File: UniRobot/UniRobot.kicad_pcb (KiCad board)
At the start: 2 copper layers, 66.5 x 65.5 mm, 11 parts, among them J1 Conn_01x01_Socket, J2 Conn_01x01_Socket, J3 Conn_01x02_Socket, K1 PR23-5V-900-1A, Q1 IRLML6344TRPBF, U1 RFM69HW

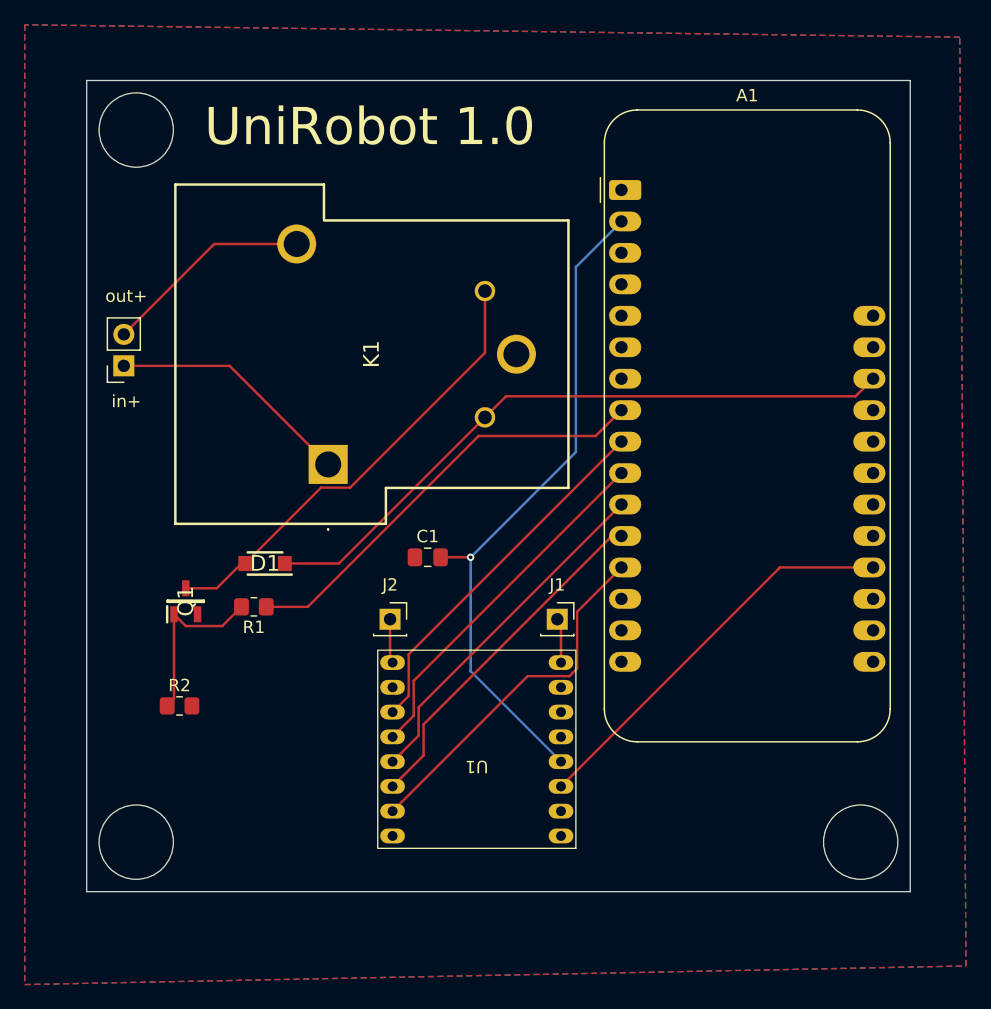
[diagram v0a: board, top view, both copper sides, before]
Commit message: Har lavet begge pcber om. Remote har ændret struktur for mere håndholdt design og ekstra knapper plus LEDer. roboside har fået ny relay og LEDer
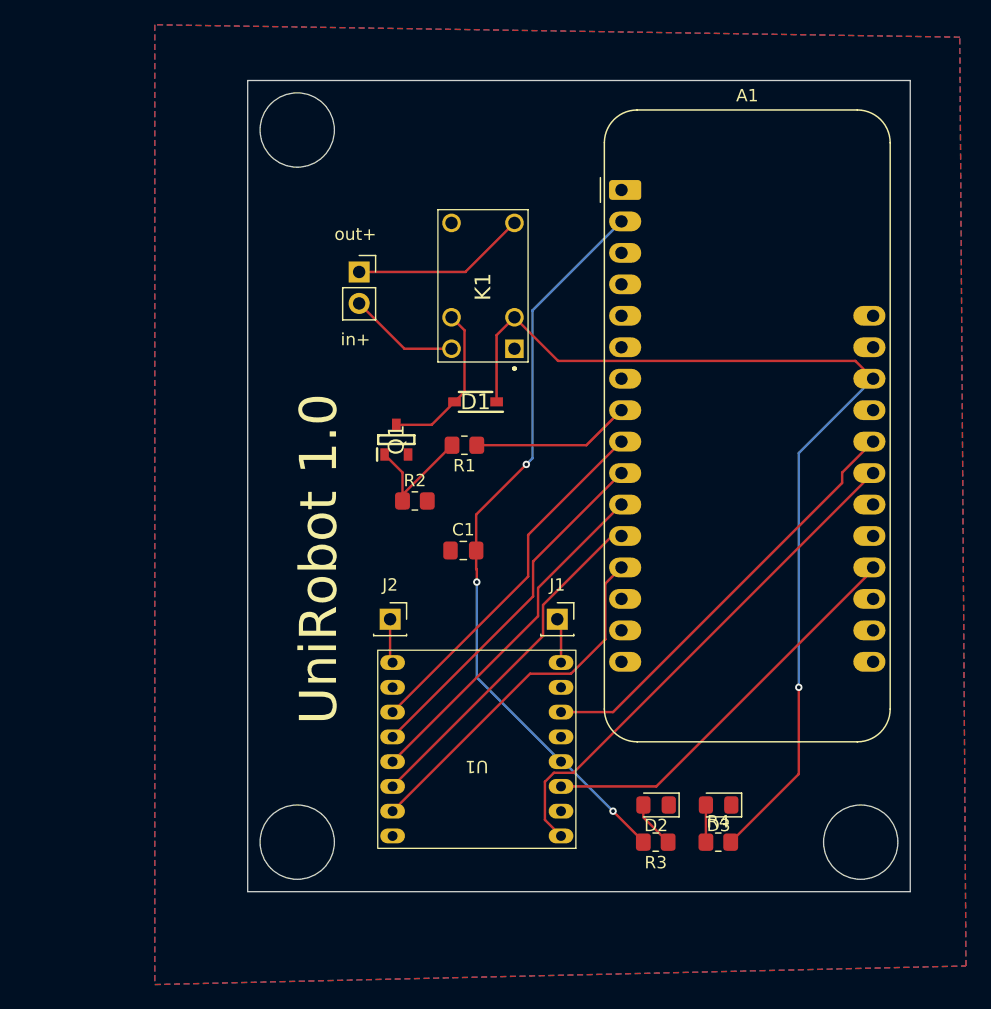
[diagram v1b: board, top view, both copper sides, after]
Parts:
- added D2: LED, LED_SMD:LED_0805_2012Metric_Pad1.15x1.40mm_HandSolder, F.Cu at (132.0, 98.5)
- added D3: LED, LED_SMD:LED_0805_2012Metric_Pad1.15x1.40mm_HandSolder, F.Cu at (137.0, 98.5)
- added R3: 280, Resistor_SMD:R_0805_2012Metric_Pad1.20x1.40mm_HandSolder, F.Cu at (131.9, 101.5)
- added R4: 620, Resistor_SMD:R_0805_2012Metric_Pad1.20x1.40mm_HandSolder, F.Cu at (137.0, 101.5)
- D1: value SL1J -> D; footprint Remote-footprints:SODFL3718X130N(diode) -> Remote-footprints:SODFL3816X120N(diode den vi har)
- K1: value PR23-5V-900-1A -> G5V-1-DC5; footprint Remote-footprints:PR235V9001A -> Remote-footprints:G5V1DC24
- Q1: value IRLML6344TRPBF -> BSS138; footprint Remote-footprints:SOT95P237X112-3N(nmosTansRelay) -> Remote-footprints:nmos
- moved R2 25.2 mm to (112.5, 74.0)
- moved D1 21.4 mm to (117.4, 66.0)
- moved Q1 21.4 mm to (111.0, 69.0)
- moved R1 21.4 mm to (116.5, 69.5)
- moved J3 20.5 mm to (108.0, 55.5), turned to 0 degrees
- moved K1 17.7 mm to (120.5, 61.7)
- moved C1 2.93 mm to (116.4, 78.0)
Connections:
- A1 pad 23: unconnected-(A1-D11-Pad23) -> DIO2
- A1 pad 24: unconnected-(A1-D12-Pad24) -> DIO3
- K1 pad 1: Net-(J3-Pin_1) -> unconnected-(K1-NC-Pad1)
- K1 pad 5: Net-(J3-Pin_2) -> Net-(J3-Pin_1)
- U1 pad 1: unconnected-(U1-DIO2-Pad1) -> DIO2
- U1 pad 6: unconnected-(U1-DIO3-Pad6) -> DIO3
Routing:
- net DIO2: track 0.00 -> 41.7 mm
- net DIO3: track 0.00 -> 34.7 mm
- net Net-(A1-USB): track 53.7 -> 80.6 mm, vias 0 -> 1
- net Net-(D1-A): track 37.0 -> 13.1 mm
- net Net-(A1-A3): track 35.3 -> 12.9 mm
- net Net-(J3-Pin_2): track 17.0 -> 8.98 mm
- net +3.3V: track 54.1 -> 60.7 mm, vias 1 -> 3
- net Net-(J3-Pin_1): track 19.8 -> 14.2 mm
- net Net-(D2-A): track 0.00 -> 3.83 mm
- net Net-(Q1-G): track 14.1 -> 10.5 mm
- net Net-(D3-A): track 0.00 -> 3.00 mm
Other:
- board size 66.5 x 65.5 mm -> 53.5 x 65.5 mm

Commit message: pcb
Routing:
- net +3.3V: track 60.7 -> 62.6 mm
- net DIO2: track 41.7 -> 40.0 mm, vias 0 -> 1
- net Net-(A1-USB): track 80.6 -> 81.8 mm, vias 1 -> 0
- net Net-(J3-Pin_1): track 14.2 -> 14.9 mm
- net DIO3: track 34.7 -> 35.4 mm
